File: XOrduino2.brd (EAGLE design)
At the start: 68.6 x 53.3 mm, 36 parts, among them Q1 2N2907, SW1 RESET, SW2 RESET, U1 ATMEGA32U4-XUAU, U2 LCD-16X2SILK, X3 USBMICROB-VIA, Y1 16MHz

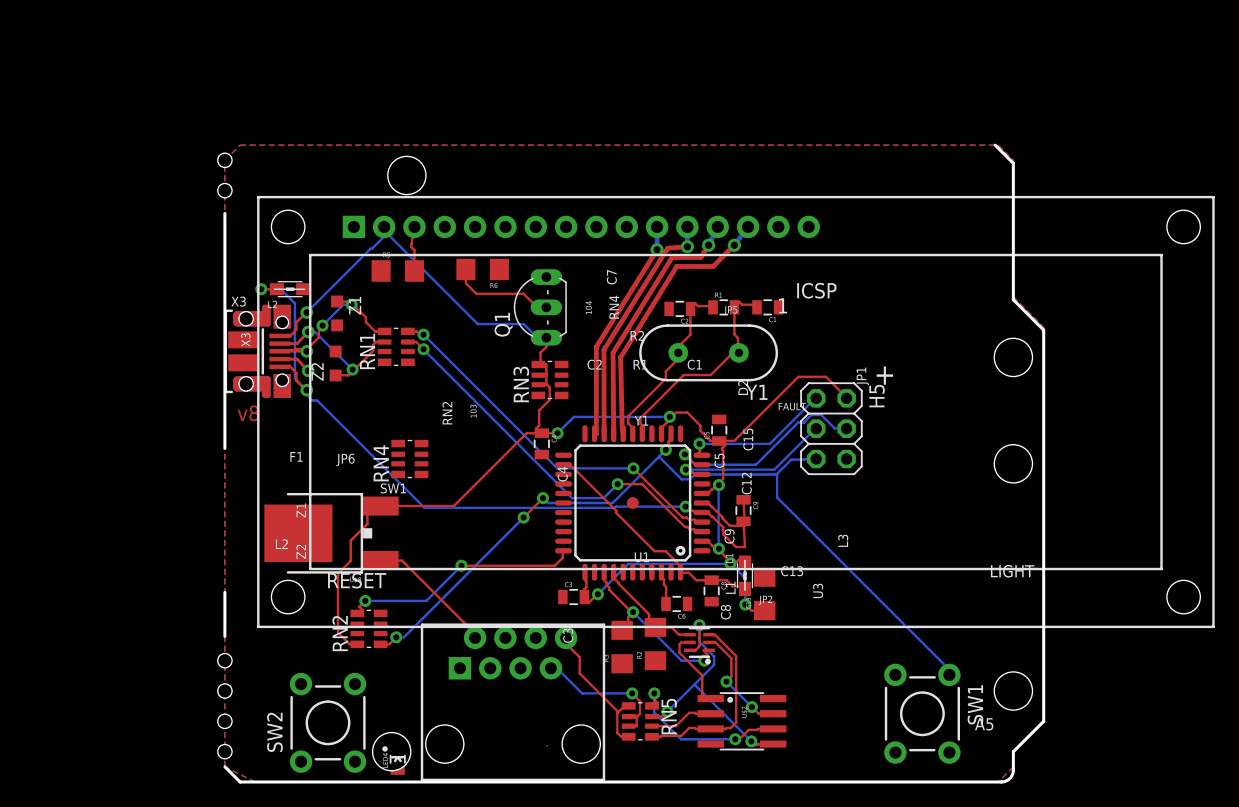
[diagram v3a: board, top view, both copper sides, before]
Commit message: changed usb connector, most of the devices are connected
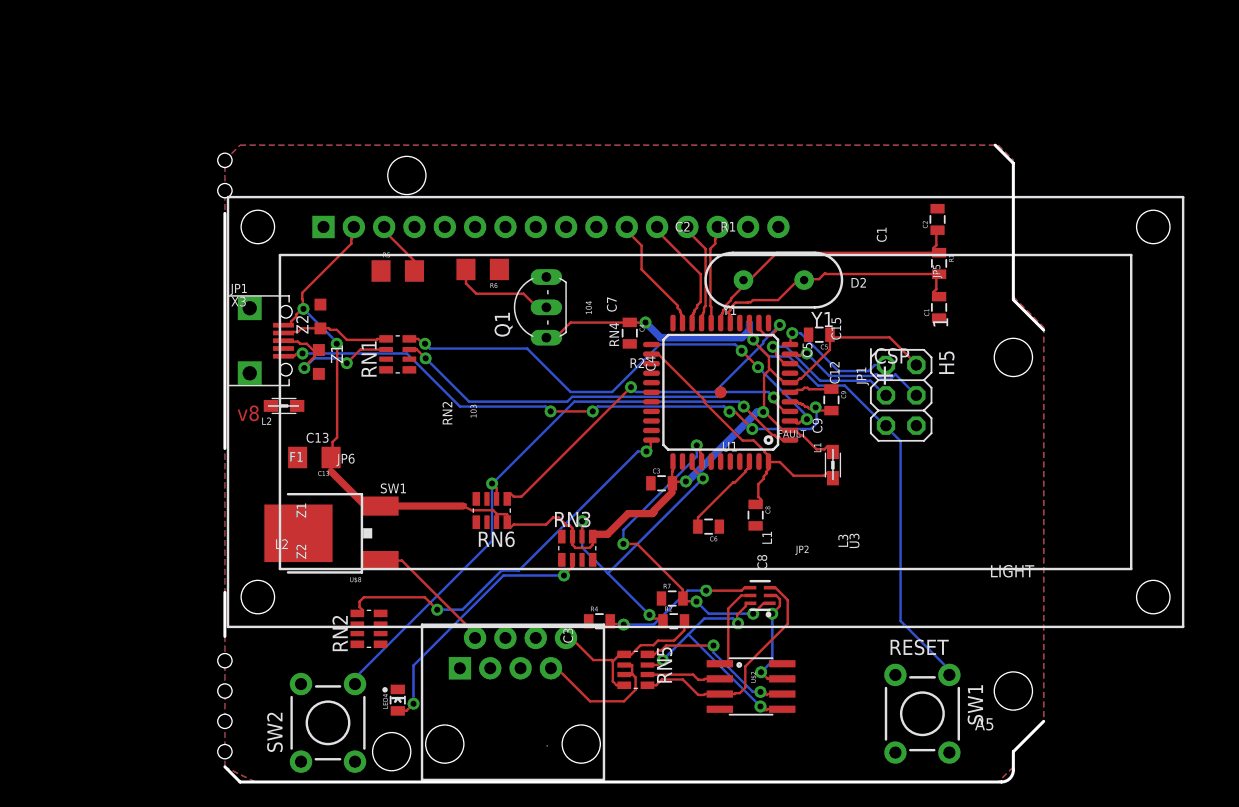
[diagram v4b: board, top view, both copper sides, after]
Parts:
- removed R3: (no value), SparkFun-Passives:1206
- removed RN4: 100k, xorduino:CRA06S
- removed X3: USBMICROB-VIA, xorduino:USB-MICROB-VIA
- added JP1: USB-RECEPTABLE, daspilker:FCI-10103594-0001LF
- added R4, R7: (no value), SparkFun-Passives:0805
- added RN6: 10k, xorduino:CRA06S
- R2: device SparkFun-Passives:1206 -> SparkFun-Passives:0805
- moved C13 39.4 mm to (20.2, 27.2), turned to 180 degrees
- moved C2 22.9 mm to (72.4, 47.1), turned to 90 degrees
- moved R1 18.4 mm to (72.5, 43.4), turned to 270 degrees
- moved C1 14.4 mm to (72.5, 39.8), turned to 90 degrees
- moved RN3 14.3 mm to (42.2, 19.6), turned to 0 degrees
- moved C3 12.0 mm to (49.3, 25.0)
- moved U1 11.8 mm to (54.2, 32.6)
- moved L1 11.8 mm to (63.6, 26.5)
- moved C4 11.8 mm to (46.6, 37.6)
- moved C9 11.8 mm to (63.5, 32.0)
- moved C5 11.6 mm to (62.5, 37.5), turned to 180 degrees
- moved L2 9.79 mm to (17.7, 31.5)
- moved Y1 8.18 mm to (58.7, 42.0)
- moved C8 7.34 mm to (57.1, 22.4)
- moved C6 7.00 mm to (53.2, 21.4)
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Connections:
- removed net A1: R2.2, U$5.4, U1.37
- removed net LED2_ANODE: RN3.3
- new net N$11: R2.1, RN3.6, U1.36
- new net N$15: JP1.4
- new net N$9: U1.38
- net +5V: now also JP1.1, RN6.7, RN6.8; no longer RN2.8, RN3.6, X3.VBUS, X3.VBUS_VIA
- net A0: now also R7.2, U1.37; no longer R3.2, U1.36
- net A2: now also R4.2, U$5.4; no longer U1.38
- net D7: now also RN6.2, SW2.4
- net D_M: now also JP1.2, RN1.5; no longer RN1.6, X3.D-, X3.D-_VIA
- net D_P: now also JP1.3, RN1.6; no longer RN1.5, X3.D+, X3.D+_VIA
- net GND: now also R4.1, R7.1, RN3.3, SW2.2; no longer R2.1, R3.1
- net N$7: now also R2.2
- net RD_M: now also RN1.4; no longer RN1.3
- net RD_P: now also RN1.3; no longer RN1.4
- net RESET: now also RN6.1; no longer RN2.1
- net UGND: now also JP1.5; no longer X3.GND, X3.GND_VIA
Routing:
- net D7: track 0.00 -> 52.1 mm, vias 0 -> 2
- net N$11: track 0.00 -> 26.0 mm, vias 0 -> 3
- net LED4_ANODE: track 0.00 -> 22.1 mm, vias 0 -> 2
- net D3/SCL: track 22.8 -> 8.34 mm, vias 1 -> 0
- net A2: track 0.00 -> 13.3 mm, vias 0 -> 2
- net D2/SDA: track 21.5 -> 8.82 mm, vias 1 -> 0
- net +5V: track 140.7 -> 128.2 mm, vias 7 -> 6
- net HWB: track 20.5 -> 32.8 mm
- net A0: track 15.8 -> 27.9 mm, vias 2 -> 4
- net D0/RX: track 20.4 -> 9.87 mm, vias 1 -> 0
- net A1: track 9.56 -> 0.00 mm
- net RD_M: track 32.2 -> 41.3 mm, vias 2 -> 4
- net D1/TX: track 18.9 -> 9.99 mm, vias 1 -> 0
- net XTAL1: track 15.4 -> 24.3 mm
- net MOSI: track 17.9 -> 12.6 mm
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
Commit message: added terminal block to sense power on
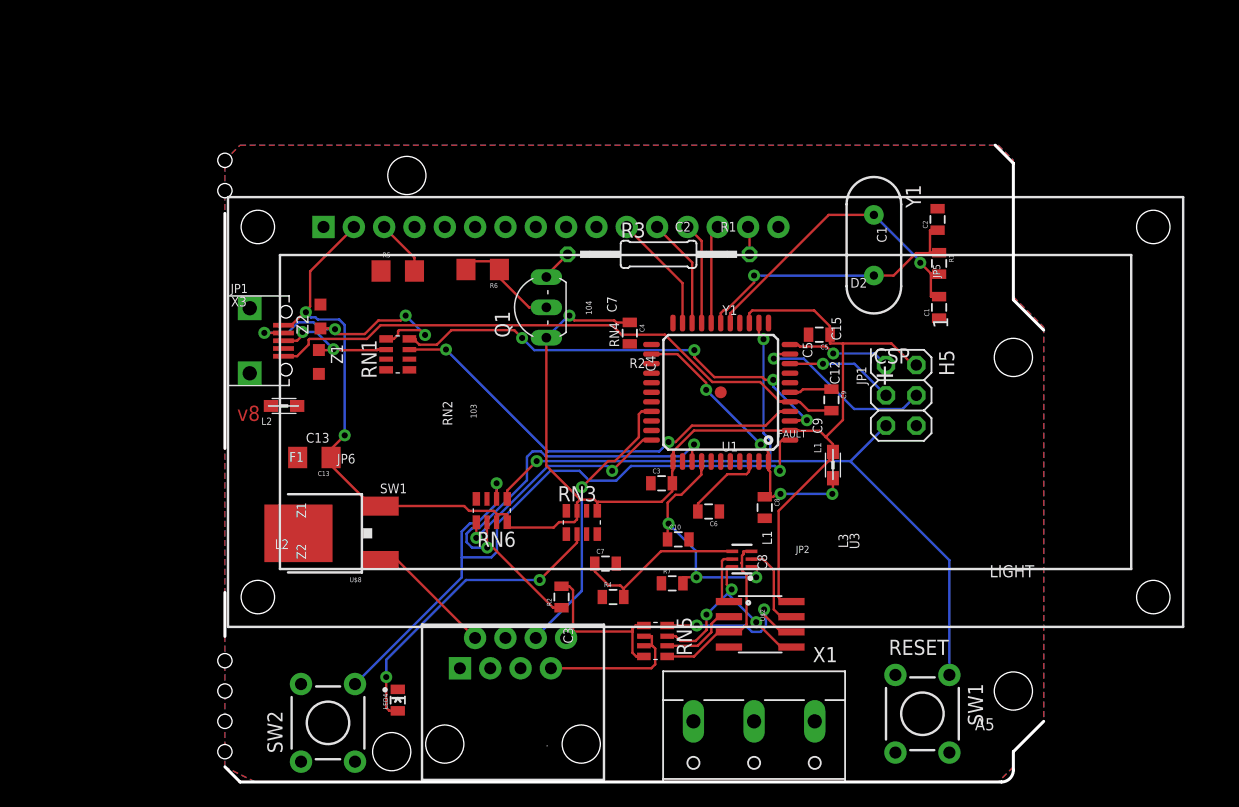
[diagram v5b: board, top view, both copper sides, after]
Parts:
- removed RN2: 10k, xorduino:CRA06S
- added C10, C7: (no value), SparkFun-Capacitors:0805
- added R3: (no value), adafruit:0207/15
- added X1: (no value), con-wago-508:W237-133
- RN5: value 22 -> 1K
- moved R2 9.62 mm to (40.9, 15.5), turned to 90 degrees
- moved Y1 8.88 mm to (67.1, 45.0), turned to 270 degrees
- moved U$2 5.26 mm to (57.5, 13.2)
- moved U$5 3.41 mm to (56.0, 18.7)
- moved RN5 2.92 mm to (48.8, 11.8)
- moved R4 2.33 mm to (45.2, 15.5)
- moved RN3 2.19 mm to (42.6, 21.7)
- moved C6 1.27 mm to (53.2, 22.7)
- moved R7 1.27 mm to (50.2, 16.6)
- moved C8 0.99 mm to (57.9, 23.0)
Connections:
- removed net +V: U$2.8
- new net N$10: Q1.C, R3.1
- new net N$16: U1.7
- new net N$20: U$6.5
- net +5V: now also U$2.8; no longer U1.7
- net A0: now also C10.1
- net A2: now also C7.1
- net GND: now also C10.2, C7.2, RN6.3, RN6.4, U$6.3, U$6.4; no longer R5.1, RN2.4, RN3.3
- net HWB: now also RN6.5; no longer RN2.5
- net IO10*: now also U$6.6
- net N$11: now also RN6.6; no longer RN3.6
- net N$13: now also R3.2
- net N$14: now also R6.1
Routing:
- net IO10*: track 0.00 -> 23.8 mm, vias 0 -> 1
- net +5V: track 128.2 -> 145.0 mm, vias 6 -> 3
- net D_M: track 9.20 -> 22.6 mm, vias 0 -> 4
- net HWB: track 32.8 -> 19.7 mm
- net N$11: track 26.0 -> 38.3 mm, vias 3 -> 2
- net D7: track 52.1 -> 58.7 mm
- net A0: track 27.9 -> 21.5 mm, vias 4 -> 3
- net N$1: track 19.9 -> 14.8 mm
- net SCK: track 13.5 -> 9.14 mm
- net N$3: track 22.3 -> 18.2 mm
- net LED4_ANODE: track 22.1 -> 25.9 mm
- net XTAL2: track 22.8 -> 26.5 mm, vias 0 -> 1
- net MOSI: track 12.6 -> 15.7 mm
- net UGND: track 53.2 -> 50.2 mm, vias 6 -> 0
- net N$4: track 7.63 -> 4.90 mm
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
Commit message: some hand routing, currently about4 air wires
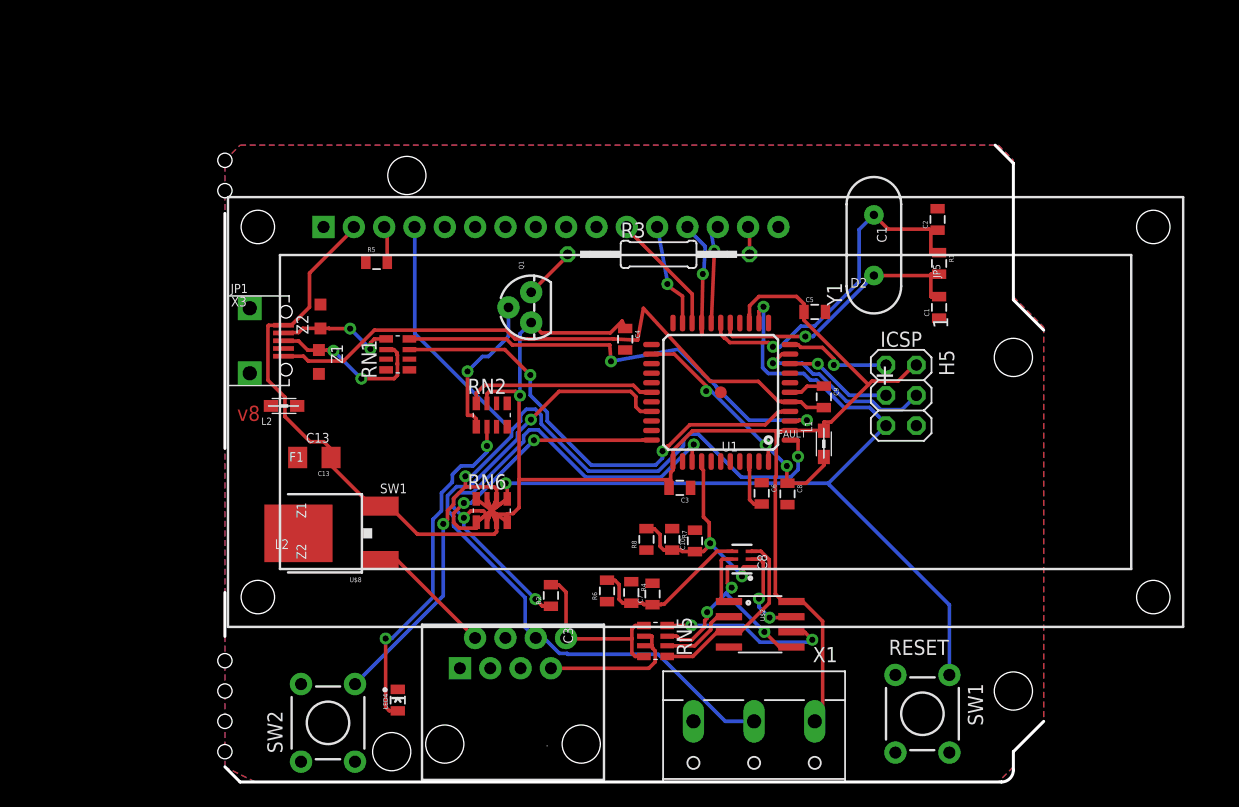
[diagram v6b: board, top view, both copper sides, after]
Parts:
- removed RN3: 1k, xorduino:CRA06S
- added R8: 47k, SparkFun-Passives:0805
- added RN2: 1k, xorduino:CRA06S
- Q1: value 2N2907 -> TRANSISTOR_PNPTO92; device adafruit:TO92-EBC-OVAL -> SparkFun-DiscreteSemi:TO-92
- R2: value (none) -> 22k
- R3: value (none) -> 47
- R4, R7: value (none) -> 47k
- R5, R6: value (none) -> 47k; device SparkFun-Passives:1206 -> SparkFun-Passives:0805
- moved R6 28.9 mm to (44.7, 16.0), turned to 90 degrees
- moved C6 4.70 mm to (57.7, 24.2), turned to 270 degrees
- moved C7 4.69 mm to (48.5, 15.7), turned to 90 degrees
- moved R7 3.68 mm to (50.2, 20.3), turned to 270 degrees
- moved C8 2.22 mm to (59.8, 24.1)
- moved C5 1.94 mm to (62.1, 39.4), turned to 0 degrees
- moved L1 1.93 mm to (62.9, 28.3)
- moved R5 1.93 mm to (25.4, 43.6)
- moved R4 1.57 mm to (46.7, 15.9), turned to 270 degrees
- moved C3 1.57 mm to (50.8, 24.6), turned to 180 degrees
- moved C10 1.40 mm to (52.1, 20.2), turned to 90 degrees
- moved R2 0.90 mm to (40.0, 15.6)
- moved C9 0.68 mm to (62.9, 32.3)
- moved C4 0.63 mm to (46.2, 37.1)
- turned RN6 to 0 degrees
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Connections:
- removed net LED3_ANODE: RN3.4
- removed net N$14: Q1.B, R6.1, R6.2
- new net D6: U2.6
- new net N$19: Q1.2, RN2.1
- net +5V: now also Q1.1, RN2.7, X1.1; no longer Q1.E, RN3.5, RN3.7
- net A0: now also R8.2
- net A2: now also R6.2
- net D0/RX: now also U2.11; no longer U2.12
- net D1/TX: now also U2.12; no longer U2.11
- net D7: now also U2.4
- net GND: now also R5.1, R6.1, R8.1, X1.3
- net IO10*: now also X1.2
- net IO8: now also RN2.8
- net LED4_ANODE: now also RN2.2; no longer RN3.2
- net N$10: now also Q1.3; no longer Q1.C
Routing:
- net IO10*: track 23.8 -> 58.3 mm
- net D7: track 58.7 -> 87.1 mm, vias 2 -> 3
- net +5V: track 145.0 -> 166.8 mm, vias 3 -> 1
- net IO8: track 0.00 -> 16.0 mm
- net D_M: track 22.6 -> 10.1 mm, vias 4 -> 2
- net N$19: track 0.00 -> 12.3 mm, vias 0 -> 1
- net RESET: track 68.0 -> 77.8 mm
- net N$14: track 9.80 -> 0.00 mm
- net N$11: track 38.3 -> 44.9 mm, vias 2 -> 3
- net HWB: track 19.7 -> 25.7 mm
- net XTAL1: track 24.1 -> 29.8 mm
- net XTAL2: track 26.5 -> 23.2 mm
- net LED4_ANODE: track 25.9 -> 29.0 mm
- net D_P: track 11.0 -> 13.9 mm
- net RD_P: track 36.8 -> 39.5 mm
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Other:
- board text removed: "103"
- board text removed: "104"
- board text removed: "A5"
- board text removed: "C12"
- board text removed: "C15"
- board text removed: "C2"
- board text removed: "C4"
- board text removed: "C5"
- board text removed: "C7"
- board text removed: "C9"
- board text removed: "IN"
- board text removed: "JP1"
- board text removed: "JP2"
- board text removed: "JP6"
- board text removed: "JP7"
- board text removed: "JP8"
- board text removed: "JP9"
- board text removed: "L1"
- board text removed: "L3"
- board text removed: "LIGHT"
- board text removed: "R1"
- board text removed: "R2"
- board text removed: "RN2"
- board text removed: "RN4"
- board text removed: "U3"
- board text removed: "U5"
- board text removed: "Y1"
